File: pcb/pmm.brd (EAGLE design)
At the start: 78.6 x 43 mm, 38 parts, among them IC3 STM32F042F4, J1 AUDIO_JACK_3.5MM_PTH, J2 FFC3B07-05-T, SW3 324_SW, SW4 324_SW, U2 USBC_16P, U4 XC6206_DEV

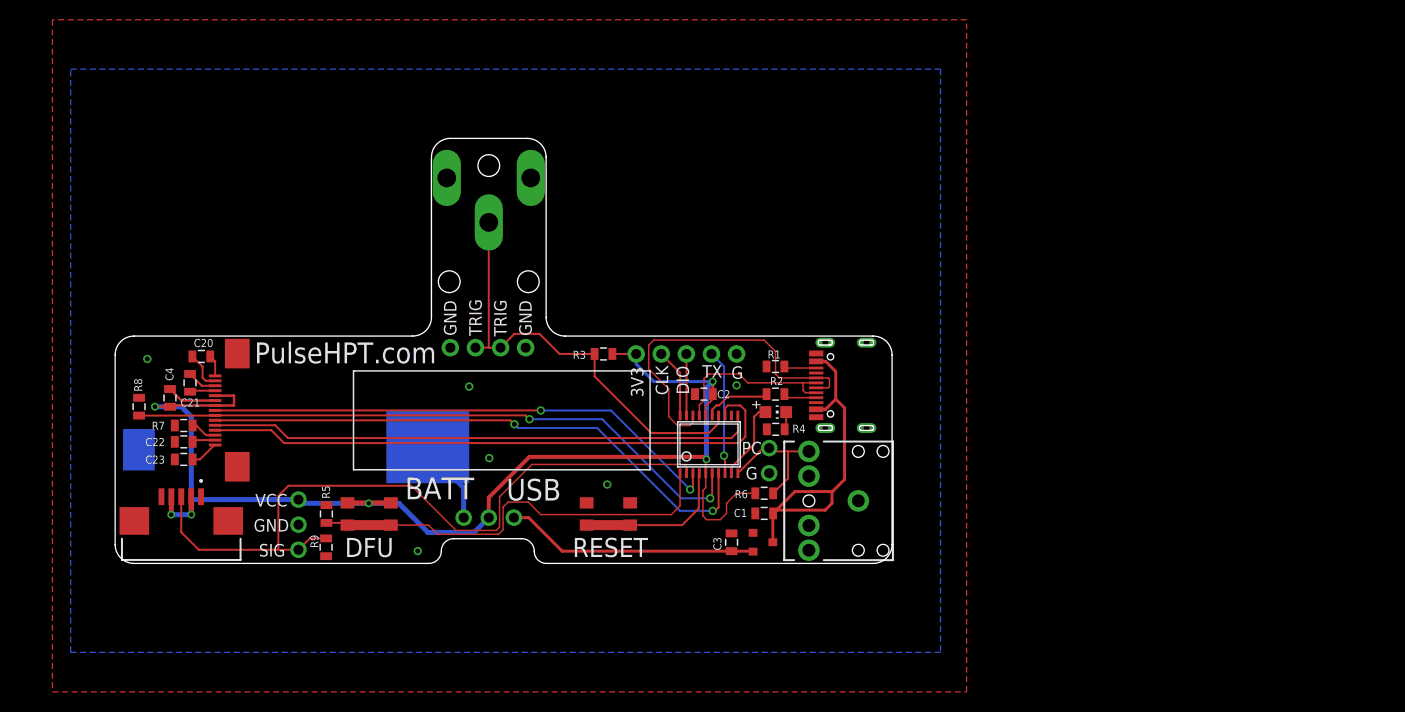
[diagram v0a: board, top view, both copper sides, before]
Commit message: added spring contacts
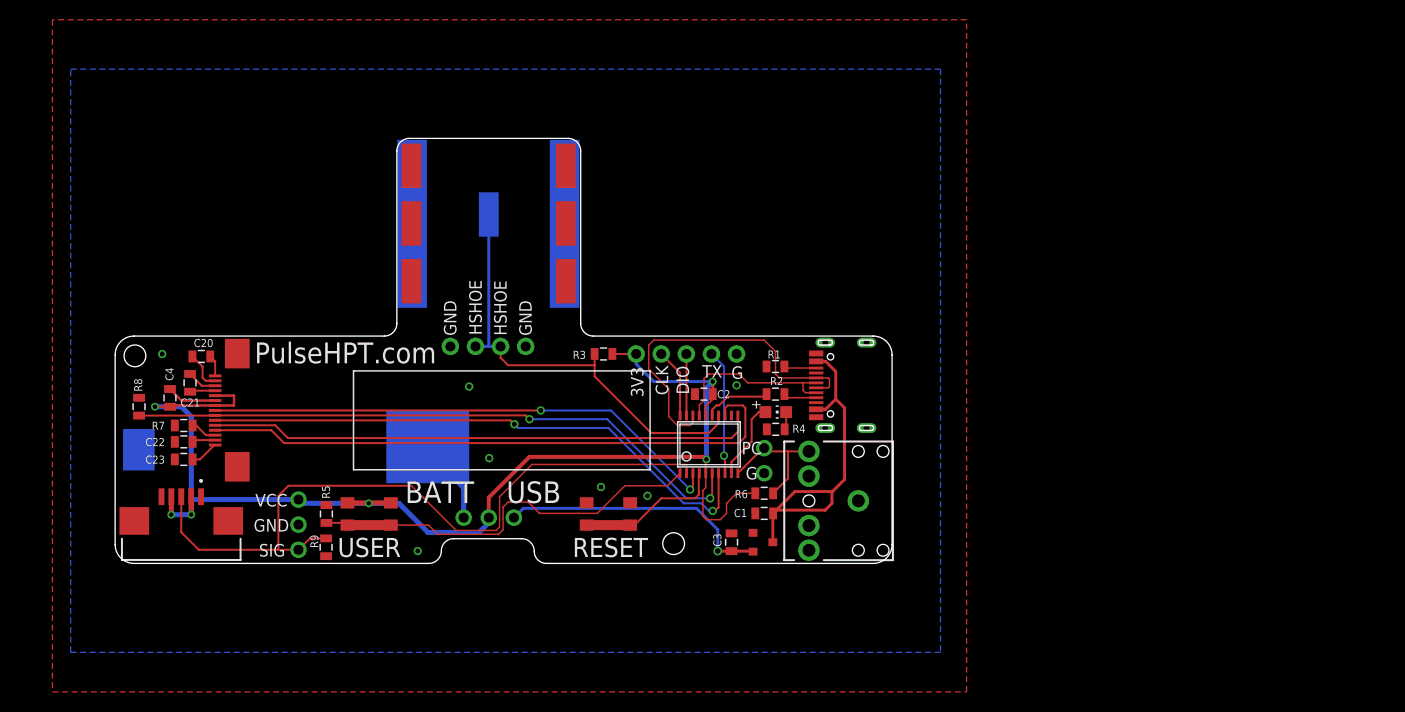
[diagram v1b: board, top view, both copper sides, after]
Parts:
- removed U$3: POGO_TH001, apricot:POGO_1.8
- added U$10, U$15: HOTSHOE, apricot:HOTSHOE_RAIL
- added U$11, U$13, U$14, U$9: SPRING_CONTACT, apricot:SPRING_CONTACT
- U$2: value M2_SCREW_DEV -> SPRING_CONTACT; device 3pos_slide_switch_centered:M2_SCREW_FOOT -> apricot:SPRING_CONTACT
- U$4, U$5: value POGO_TH001 -> SPRING_CONTACT; device apricot:POGO_1.8 -> apricot:SPRING_CONTACT
- moved U$12 40.6 mm to (-29.5, -4.00)
- moved U$1 30.3 mm to (25.0, -23.0)
- moved U$4 12.1 mm to (14.1, 15.2)
- moved U$2 7.89 mm to (6.30, 10.3), flipped to the bottom
- moved U$5 5.81 mm to (14.1, 9.40)
- moved U$8 0.51 mm to (34.2, -14.6)
- moved U$7 0.13 mm to (6.22, -3.05)
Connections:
- net GND: now also U$10.P$1, U$11.P$1, U$13.P$1, U$14.P$1, U$15.P$1, U$9.P$1
- net N$2: now also U$2.P$1; no longer U$3.P$1
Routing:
- net N$3: track 25.6 -> 27.7 mm, vias 0 -> 1
- net BUTTON2: track 43.1 -> 41.1 mm
- net BUTTON1: track 15.6 -> 14.8 mm
- net N$2: track 44.5 -> 45.3 mm
- net GND: vias 6 -> 7
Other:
- outline, holes or cut-outs redrawn
- board text added: "HSHOE"
- board text added: "USER"
- board text removed: "DFU"
- board text removed: "TRIG"

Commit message: pcb cleanup
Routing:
- net N$3: track 27.7 -> 27.1 mm
- net GND: vias 7 -> 6
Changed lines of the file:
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@@
 <contactref element="R4" pad="1"/>
 <via x="4.318" y="-7.112" extent="1-16" drill="0.5"/>
-<via x="17.653" y="-17.272" extent="1-16" drill="0.5"/>
 <via x="6.35" y="-14.351" extent="1-16" drill="0.5"/>
 <via x="-26.742" y="-3.818" extent="1-16" drill="0.5"/>
@@
 <contactref element="U$10" pad="P$1"/>
 <contactref element="U$15" pad="P$1"/>
-<via x="22.352" y="-18.161" extent="1-16" drill="0.5"/>
+<via x="18.415" y="-17.272" extent="1-16" drill="0.5"/>
 </signal>
 <signal name="+3V3">
@@
 <wire x1="-10.1286" y1="-20.9" x2="-8.225" y2="-20.9" width="0.2" layer="1"/>
 <wire x1="-8.225" y1="-20.9" x2="-8" y2="-21.125" width="0.2" layer="1"/>
-<wire x1="11.43" y1="-19.939" x2="10.287" y2="-18.796" width="0.1524" layer="1"/>
 <wire x1="0.211" y1="-21.125" x2="-3.6" y2="-21.125" width="0.1524" layer="1"/>
-<wire x1="10.287" y1="-18.796" x2="8.255" y2="-18.796" width="0.1524" layer="1"/>
 <wire x1="1.1332" y1="-22.0472" x2="0.211" y2="-21.125" width="0.1524" layer="1"/>
 <wire x1="1.1332" y1="-22.0472" x2="7.2898" y2="-22.0472" width="0.1524" layer="1"/>
-<wire x1="8.255" y1="-18.796" x2="7.747" y2="-19.304" width="0.1524" layer="1"/>
 <wire x1="7.747" y1="-21.59" x2="7.2898" y2="-22.0472" width="0.1524" layer="1"/>
-<wire x1="7.747" y1="-19.304" x2="7.747" y2="-21.59" width="0.1524" layer="1"/>
-<wire x1="25.65" y1="-15.8718" x2="24.3768" y2="-17.145" width="0.1524" layer="1"/>
-<wire x1="17.272" y1="-19.939" x2="11.43" y2="-19.939" width="0.1524" layer="1"/>
-<wire x1="24.3768" y1="-17.145" x2="20.066" y2="-17.145" width="0.1524" layer="1"/>
-<wire x1="20.066" y1="-17.145" x2="17.272" y2="-19.939" width="0.1524" layer="1"/>
+<wire x1="7.747" y1="-21.59" x2="7.747" y2="-18.669" width="0.1524" layer="1"/>
+<wire x1="7.747" y1="-18.669" x2="10.7982" y2="-15.6178" width="0.1524" layer="1"/>
+<wire x1="25.396" y1="-15.6178" x2="25.65" y2="-15.8718" width="0.1524" layer="1"/>
+<wire x1="25.396" y1="-15.6178" x2="10.7982" y2="-15.6178" width="0.1524" layer="1"/>
 </signal>
 <signal name="N$5">
@@
 <wire x1="8.493" y1="-10.525" x2="8.89" y2="-10.922" width="0.2032" layer="1"/>
 <via x="8.89" y="-10.922" extent="1-16" drill="0.5"/>
-<wire x1="18.415" y1="-11.303" x2="9.271" y2="-11.303" width="0.2032" layer="16"/>
+<wire x1="18.034" y1="-11.303" x2="9.271" y2="-11.303" width="0.2032" layer="16"/>
 <wire x1="8.89" y1="-10.922" x2="9.271" y2="-11.303" width="0.2032" layer="16"/>
 <wire x1="28.575" y1="-19.685" x2="28.956" y2="-19.685" width="0.2032" layer="16"/>
-<wire x1="28.575" y1="-19.685" x2="27.813" y2="-18.923" width="0.2032" layer="16"/>
-<wire x1="27.813" y1="-18.923" x2="26.035" y2="-18.923" width="0.2032" layer="16"/>
+<wire x1="28.575" y1="-19.685" x2="27.94" y2="-19.05" width="0.2032" layer="16"/>
+<wire x1="27.94" y1="-19.05" x2="25.781" y2="-19.05" width="0.2032" layer="16"/>
 <via x="28.956" y="-19.685" extent="1-16" drill="0.5"/>
 <wire x1="29.55" y1="-19.345" x2="29.21" y2="-19.685" width="0.2032" layer="1"/>
 <wire x1="28.956" y1="-19.685" x2="29.21" y2="-19.685" width="0.2032" layer="1"/>
 <wire x1="29.55" y1="-19.345" x2="29.55" y2="-15.8718" width="0.2032" layer="1"/>
-<wire x1="18.415" y1="-11.303" x2="26.035" y2="-18.923" width="0.2032" layer="16"/>
+<wire x1="18.034" y1="-11.303" x2="25.781" y2="-19.05" width="0.2032" layer="16"/>
 </signal>
 <signal name="OLED_CS">
@@
 <wire x1="-1.524" y1="-17.145" x2="2.9972" y2="-21.6662" width="0.1524" layer="1"/>
 <wire x1="2.9972" y1="-21.6662" x2="7.0358" y2="-21.6662" width="0.1524" layer="1"/>
-<wire x1="10.668" y1="-14.986" x2="26.162" y2="-14.986" width="0.1524" layer="1"/>
+<wire x1="10.795" y1="-14.859" x2="26.162" y2="-14.859" width="0.1524" layer="1"/>
 <wire x1="7.0358" y1="-21.6662" x2="7.3914" y2="-21.3106" width="0.1524" layer="1"/>
 <wire x1="7.3914" y1="-21.3106" x2="7.3914" y2="-18.2626" width="0.1524" layer="1"/>
-<wire x1="7.3914" y1="-18.2626" x2="10.668" y2="-14.986" width="0.1524" layer="1"/>
+<wire x1="7.3914" y1="-18.2626" x2="10.795" y2="-14.859" width="0.1524" layer="1"/>
 <contactref element="IC3" pad="2"/>
-<wire x1="26.162" y1="-14.986" x2="26.3" y2="-15.124" width="0.1524" layer="1"/>
-<wire x1="26.3" y1="-15.124" x2="26.3" y2="-15.8718" width="0.1524" layer="1"/>
+<wire x1="26.162" y1="-14.859" x2="26.3" y2="-14.997" width="0.1524" layer="1"/>
+<wire x1="26.3" y1="-14.997" x2="26.3" y2="-15.8718" width="0.1524" layer="1"/>
 <contactref element="JP2" pad="1"/>
 <contactref element="R9" pad="1"/>
@@
 <wire x1="29.475" y1="-23.76" x2="29.464" y2="-23.749" width="0.3048" layer="1"/>
 <via x="29.464" y="-23.749" extent="1-16" drill="0.55"/>
-<wire x1="29.464" y1="-23.749" x2="29.464" y2="-21.59" width="0.3048" layer="16"/>
-<wire x1="29.464" y1="-21.59" x2="27.305" y2="-19.431" width="0.3048" layer="16"/>
-<wire x1="9.782" y1="-19.431" x2="8.84" y2="-20.373" width="0.3048" layer="16"/>
-<wire x1="27.305" y1="-19.431" x2="9.782" y2="-19.431" width="0.3048" layer="16"/>
+<wire x1="29.464" y1="-23.749" x2="29.464" y2="-22.225" width="0.3048" layer="16"/>
+<wire x1="29.464" y1="-22.225" x2="26.924" y2="-19.685" width="0.3048" layer="16"/>
+<wire x1="9.528" y1="-19.685" x2="8.84" y2="-20.373" width="0.3048" layer="16"/>
+<wire x1="26.924" y1="-19.685" x2="9.528" y2="-19.685" width="0.3048" layer="16"/>
 </signal>
 <signal name="PC_SYNC">

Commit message: pcb cleanup
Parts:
- moved R9 6.07 mm to (-13.8, -18.5), turned to 180 degrees
- moved JP2 2.77 mm to (-12.2, -23.7), turned to 180 degrees
- moved R5 0.25 mm to (-10.1, -19.7)
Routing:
- net LIGHT_SENSE: track 74.0 -> 68.1 mm
- net +3V3: track 130.1 -> 134.3 mm
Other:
- board text added: "OFF"
- board text added: "ON"
- board text added: "S"
- board text added: "V"
- board text removed: "BATT"
- board text removed: "SIG"
- board text removed: "USB"
- board text removed: "VCC"
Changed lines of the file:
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@@
 <text x="4.953" y="0.889" size="1.27" layer="25" rot="R270" align="center">HSHOE</text>
 <text x="2.3944" y="-0.1782" size="1.27" layer="25" rot="R270" align="center">GND</text>
-<text x="-5.7908" y="-23.3866" size="1.9304" layer="25" align="center">USER</text>
+<text x="-5.1558" y="-23.5136" size="1.9304" layer="25" align="center">USER</text>
 <text x="18.5932" y="-23.3866" size="1.9304" layer="25" align="center">RESET</text>
-<text x="1.3212" y="-17.7986" size="2.1844" layer="25" align="center">BATT</text>
-<text x="10.8462" y="-17.7986" size="2.1844" layer="25" align="center">USB</text>
+<text x="1.8292" y="-17.7986" size="2.1844" layer="25" align="center">ON</text>
+<text x="10.4652" y="-17.7986" size="2.1844" layer="25" align="center">OFF</text>
 <rectangle x1="-4.064" y1="-16.891" x2="4.318" y2="-9.525" layer="16"/>
-<text x="32.893" y="-13.335" size="1.27" layer="25" align="center">PC</text>
-<text x="32.893" y="-15.875" size="1.27" layer="25" rot="R180" align="center">G</text>
-<text x="-15.621" y="-23.67" size="1.27" layer="25" rot="R180" align="center">SIG</text>
-<text x="-15.6968" y="-21.1486" size="1.27" layer="25" align="center">GND</text>
-<text x="-15.6968" y="-18.6086" size="1.27" layer="25" align="center">VCC</text>
+<text x="32.639" y="-13.208" size="1.27" layer="25" rot="R90" align="center">PC</text>
+<text x="32.639" y="-15.875" size="1.27" layer="25" align="center">G</text>
+<text x="-9.652" y="-22.019" size="1.27" layer="25" rot="R180" align="center">S</text>
+<text x="-12.1408" y="-22.0376" size="1.27" layer="25" align="center">G</text>
+<text x="-14.6808" y="-22.0376" size="1.27" layer="25" align="center">V</text>
 <text x="-8.2038" y="-3.7016" size="2.1082" layer="25" align="center">PulseHPT.com</text>
 <text x="14.6562" y="-13.6076" size="2.1082" layer="26" rot="MR0" align="center">PulseHPT.com
@@
 <attribute name="NAME" x="37.0074" y="-11.7769" size="0.8128" layer="25"/>
 </element>
-<element name="R5" library="joyAnalog" package="0805" value="10K" x="-10.1286" y="-20" smashed="yes" rot="R270">
-<attribute name="NAME" x="-9.7641" y="-18.4544" size="0.8128" layer="25" rot="R90"/>
+<element name="R5" library="joyAnalog" package="0805" value="10K" x="-10.1286" y="-19.746" smashed="yes" rot="R270">
+<attribute name="NAME" x="-9.7641" y="-18.2004" size="0.8128" layer="25" rot="R90"/>
 </element>
 <element name="U4" library="3pos_slide_switch" package="SOT23R_INFINEON" value="XC6206_DEV" x="34.036" y="-22.86" smashed="yes" rot="R270"/>
@@
 <attribute name="NAME" x="29.0195" y="-21.971" size="0.8128" layer="25" rot="R270"/>
 </element>
-<element name="JP2" library="adafruit_changed" package="1X03-CLEANBIG" value="" x="-12.954" y="-21.082" smashed="yes" rot="R90">
-<attribute name="VALUE" x="-9.779" y="-24.892" size="1.27" layer="27" rot="R90"/>
-</element>
-<element name="R9" library="joyAnalog" package="0805" value="10K" x="-10.16" y="-23.368" smashed="yes" rot="R270">
-<attribute name="NAME" x="-11.7475" y="-22.098" size="0.8128" layer="25" rot="R270"/>
+<element name="JP2" library="adafruit_changed" package="1X03-CLEANBIG" value="" x="-12.192" y="-23.749" smashed="yes" rot="R180">
+<attribute name="VALUE" x="-8.382" y="-20.574" size="1.27" layer="27" rot="R180"/>
+</element>
+<element name="R9" library="joyAnalog" package="0805" value="10K" x="-13.843" y="-18.542" smashed="yes" rot="R180">
+<attribute name="NAME" x="-13.208" y="-16.7005" size="0.8128" layer="25" rot="R180"/>
 </element>
 <element name="U$11" library="apricot" package="SPRING_CONTACT" value="SPRING_CONTACT" x="-1.524" y="3.556" smashed="yes"/>
@@
 <contactref element="JP2" pad="2"/>
 <contactref element="R9" pad="2"/>
-<via x="-0.889" y="-23.749" extent="1-16" drill="0.5"/>
+<via x="-0.381" y="-23.495" extent="1-16" drill="0.5"/>
 <contactref element="U$13" pad="P$1"/>
 <contactref element="U$11" pad="P$1"/>
@@
 <wire x1="28.967" y1="-8.371" x2="28.967" y2="-7.874" width="0.2032" layer="1"/>
 <wire x1="-27.48" y1="-9.144" x2="-24.813" y2="-9.144" width="0.508" layer="16"/>
-<wire x1="-23.797" y1="-10.16" x2="-23.797" y2="-18.542" width="0.508" layer="16"/>
-<wire x1="-23.797" y1="-18.542" x2="-23.797" y2="-20.066" width="0.508" layer="16"/>
+<wire x1="-23.797" y1="-10.16" x2="-23.797" y2="-20.066" width="0.508" layer="16"/>
 <wire x1="-24.813" y1="-9.144" x2="-23.797" y2="-10.16" width="0.508" layer="16"/>
 <wire x1="18.807" y1="-3.81" x2="21.209" y2="-3.81" width="0.2032" layer="1"/>
 <contactref element="JP2" pad="3"/>
-<wire x1="-5.842" y1="-18.923" x2="-12.573" y2="-18.923" width="0.508" layer="16"/>
-<wire x1="-12.573" y1="-18.923" x2="-12.954" y2="-18.542" width="0.508" layer="16"/>
-<wire x1="-12.954" y1="-18.542" x2="-23.797" y2="-18.542" width="0.508" layer="16"/>
+<wire x1="-5.842" y1="-18.923" x2="-11.303" y2="-18.923" width="0.508" layer="16"/>
+<wire x1="-14.732" y1="-22.352" x2="-14.732" y2="-23.749" width="0.508" layer="16"/>
+<wire x1="-11.303" y1="-18.923" x2="-14.732" y2="-22.352" width="0.508" layer="16"/>
+<wire x1="-14.732" y1="-23.749" x2="-20.114" y2="-23.749" width="0.508" layer="16"/>
+<wire x1="-20.114" y1="-23.749" x2="-23.797" y2="-20.066" width="0.508" layer="16"/>
 </signal>
 <signal name="USB_DP">
@@
 <wire x1="20.6" y1="-21.125" x2="16.2" y2="-21.125" width="1.016" layer="1"/>
 <wire x1="27.5492" y1="-18.0438" x2="27.178" y2="-18.415" width="0.2032" layer="1"/>
-<wire x1="23.749" y1="-18.415" x2="21.039" y2="-21.125" width="0.2032" layer="1"/>
-<wire x1="21.039" y1="-21.125" x2="20.6" y2="-21.125" width="0.2032" layer="1"/>
-<wire x1="27.178" y1="-18.415" x2="23.749" y2="-18.415" width="0.2032" layer="1"/>
+<wire x1="24.511" y1="-18.415" x2="21.801" y2="-21.125" width="0.2032" layer="1"/>
+<wire x1="21.801" y1="-21.125" x2="20.6" y2="-21.125" width="0.2032" layer="1"/>
+<wire x1="27.178" y1="-18.415" x2="24.511" y2="-18.415" width="0.2032" layer="1"/>
 </signal>
 <signal name="BUTTON2">
@@
 <contactref element="R5" pad="2"/>
 <wire x1="-3.6" y1="-21.125" x2="-8" y2="-21.125" width="1.016" layer="1"/>
-<wire x1="-10.1286" y1="-20.9" x2="-8.225" y2="-20.9" width="0.2" layer="1"/>
-<wire x1="-8.225" y1="-20.9" x2="-8" y2="-21.125" width="0.2" layer="1"/>
+<wire x1="-10.1286" y1="-20.646" x2="-8.479" y2="-20.646" width="0.2" layer="1"/>
+<wire x1="-8.479" y1="-20.646" x2="-8" y2="-21.125" width="0.2" layer="1"/>
 <wire x1="0.211" y1="-21.125" x2="-3.6" y2="-21.125" width="0.1524" layer="1"/>
 <wire x1="1.1332" y1="-22.0472" x2="0.211" y2="-21.125" width="0.1524" layer="1"/>
@@
 <signal name="LIGHT_SENSE">
 <contactref element="J2" pad="3"/>
-<wire x1="-24.813" y1="-18.251" x2="-24.813" y2="-21.844" width="0.2032" layer="1"/>
-<wire x1="-1.524" y1="-17.145" x2="2.9972" y2="-21.6662" width="0.1524" layer="1"/>
+<wire x1="-1.27" y1="-17.399" x2="2.9972" y2="-21.6662" width="0.1524" layer="1"/>
 <wire x1="2.9972" y1="-21.6662" x2="7.0358" y2="-21.6662" width="0.1524" layer="1"/>
 <wire x1="10.795" y1="-14.859" x2="26.162" y2="-14.859" width="0.1524" layer="1"/>
@@
 <contactref element="JP2" pad="1"/>
 <contactref element="R9" pad="1"/>
-<wire x1="-24.813" y1="-21.844" x2="-23.035" y2="-23.622" width="0.2032" layer="1"/>
-<wire x1="-13.97" y1="-17.145" x2="-14.986" y2="-18.161" width="0.2032" layer="1"/>
-<wire x1="-1.524" y1="-17.145" x2="-13.97" y2="-17.145" width="0.2032" layer="1"/>
-<wire x1="-23.035" y1="-23.622" x2="-14.986" y2="-23.622" width="0.2032" layer="1"/>
-<wire x1="-14.986" y1="-23.622" x2="-12.954" y2="-23.622" width="0.2032" layer="1"/>
-<wire x1="-12.954" y1="-23.622" x2="-11.8" y2="-22.468" width="0.2032" layer="1"/>
-<wire x1="-11.8" y1="-22.468" x2="-10.16" y2="-22.468" width="0.2032" layer="1"/>
-<wire x1="-14.986" y1="-18.161" x2="-14.986" y2="-23.622" width="0.2032" layer="1"/>
+<wire x1="-1.27" y1="-17.399" x2="-12.954" y2="-17.399" width="0.2032" layer="1"/>
+<wire x1="-12.954" y1="-17.399" x2="-14.732" y2="-17.399" width="0.2032" layer="1"/>
+<wire x1="-14.732" y1="-17.399" x2="-21.336" y2="-17.399" width="0.2032" layer="1"/>
+<wire x1="-24.813" y1="-18.251" x2="-24.813" y2="-16.812" width="0.2032" layer="1"/>
+<wire x1="-24.813" y1="-16.812" x2="-24.511" y2="-16.51" width="0.2032" layer="1"/>
+<wire x1="-24.511" y1="-16.51" x2="-22.225" y2="-16.51" width="0.2032" layer="1"/>
+<wire x1="-22.225" y1="-16.51" x2="-21.336" y2="-17.399" width="0.2032" layer="1"/>
+<wire x1="-14.743" y1="-17.41" x2="-14.732" y2="-17.399" width="0.2032" layer="1"/>
+<wire x1="-12.943" y1="-20.458" x2="-12.943" y2="-18.542" width="0.2032" layer="1"/>
+<wire x1="-9.652" y1="-23.749" x2="-12.943" y2="-20.458" width="0.2032" layer="1"/>
+<wire x1="-12.943" y1="-18.542" x2="-12.954" y2="-18.531" width="0.2032" layer="1"/>
+<wire x1="-12.954" y1="-18.531" x2="-12.954" y2="-17.399" width="0.2032" layer="1"/>
 </signal>
 <signal name="VBAT">

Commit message: adjusted resistor values
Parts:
- R7: value 390K -> 270K
- R9: value 10K -> 270K
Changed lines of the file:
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@@
 <element name="U$1" library="3pos_slide_switch_centered" package="M2_SCREW_FOOT" value="M2_SCREW_DEV" x="25" y="-23" smashed="yes"/>
 <element name="U1" library="lul" package="LUL_UG-2864HSWEG01_1.3_WRAPAROUND" value="" x="-21.384" y="-9.525" smashed="yes" rot="R90"/>
-<element name="R7" library="SparkFun-Passives" package="0805" value="390K" x="-24.559" y="-11.049" smashed="yes">
+<element name="R7" library="SparkFun-Passives" package="0805" value="270K" x="-24.559" y="-11.049" smashed="yes">
 <attribute name="NAME" x="-26.464" y="-10.668" size="0.8128" layer="25" rot="R180"/>
 </element>
@@
 <attribute name="VALUE" x="-8.382" y="-20.574" size="1.27" layer="27" rot="R180"/>
 </element>
-<element name="R9" library="joyAnalog" package="0805" value="10K" x="-13.843" y="-18.542" smashed="yes" rot="R180">
+<element name="R9" library="joyAnalog" package="0805" value="270K" x="-13.843" y="-18.542" smashed="yes" rot="R180">
 <attribute name="NAME" x="-13.208" y="-16.7005" size="0.8128" layer="25" rot="R180"/>
 </element>
